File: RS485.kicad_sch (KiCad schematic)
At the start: 8 parts, among them J7 RS485, U9 XR3072XIDTR-F

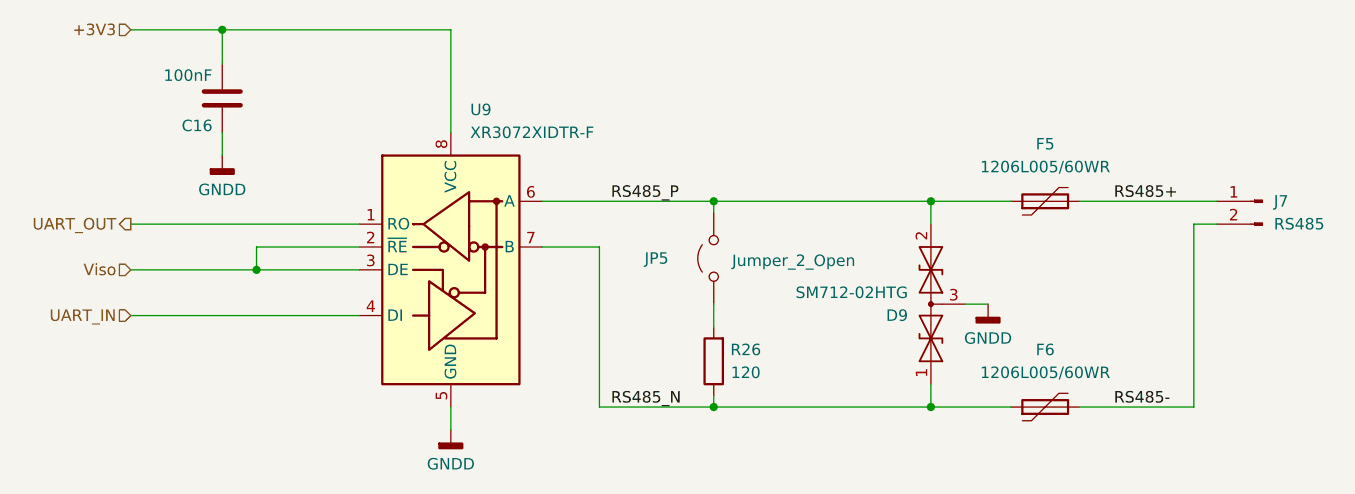
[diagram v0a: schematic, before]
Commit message: Dual SIM version
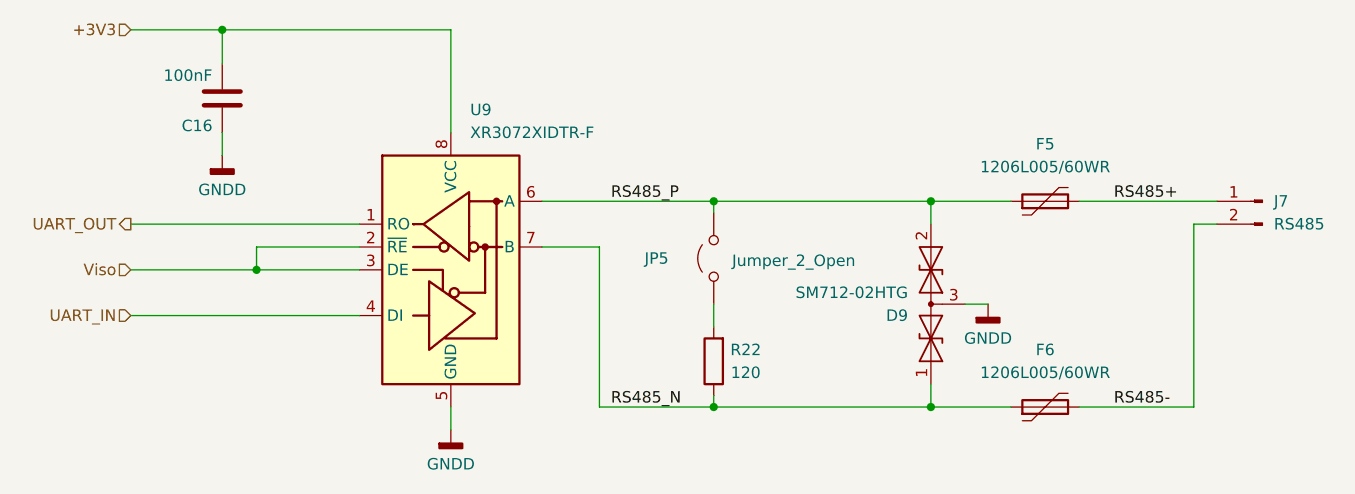
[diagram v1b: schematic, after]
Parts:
- renumbered R26 to R22
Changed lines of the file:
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@@
 		(in_pos_files yes)
 		(dnp no)
-		(property "Reference" "R26"
+		(property "Reference" "R22"
 			(at 154.686 100.33 0)
 			(show_name no)
@@
 			(project "GSMreceiver"
 				(path "/bbc92722-7b85-49e8-a662-589426df605a/fe2eac04-096c-41cd-9d48-0aafc9873100"
-					(reference "R26")
+					(reference "R22")
 					(unit 1)
 				)

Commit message: Replace SIM800C-DS with A7682E
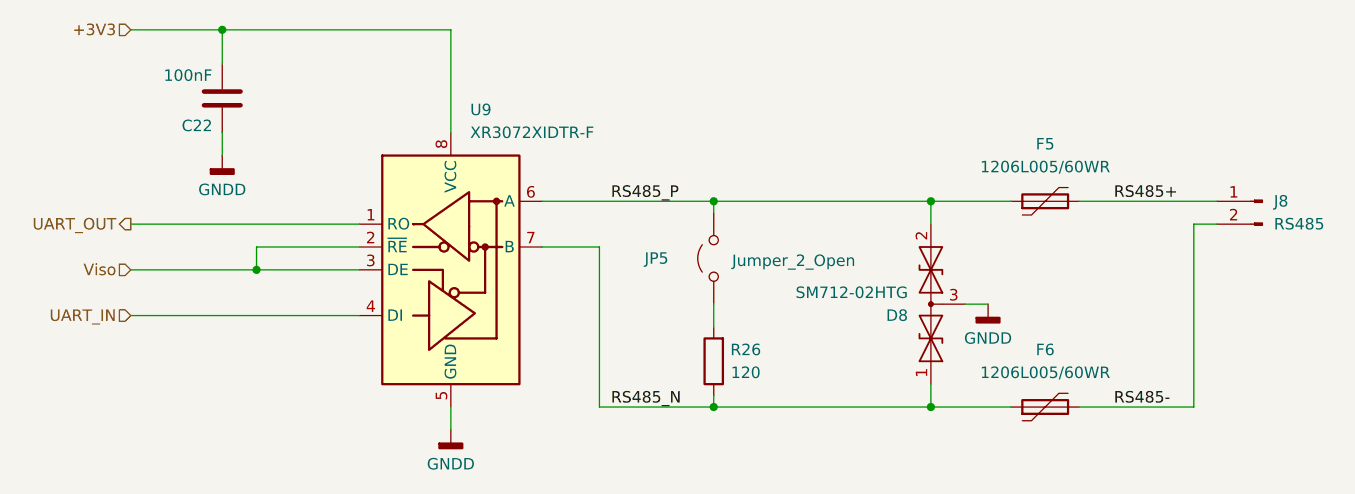
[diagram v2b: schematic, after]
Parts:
- renumbered C16 to C22, D9 to D8, J7 to J8, R22 to R26
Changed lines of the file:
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@@
 		(dnp no)
 		(fields_autoplaced yes)
-		(property "Reference" "#PWR036"
+		(property "Reference" "#PWR040"
 			(at 121.92 115.57 0)
 			(hide yes)
@@
 			(project "GSMreceiver"
 				(path "/bbc92722-7b85-49e8-a662-589426df605a/fe2eac04-096c-41cd-9d48-0aafc9873100"
-					(reference "#PWR036")
+					(reference "#PWR040")
 					(unit 1)
 				)
@@
 		(dnp no)
 		(fields_autoplaced yes)
-		(property "Reference" "D9"
+		(property "Reference" "D8"
 			(at 172.72 96.5201 90)
 			(show_name no)
@@
 			(project "GSMreceiver"
 				(path "/bbc92722-7b85-49e8-a662-589426df605a/fe2eac04-096c-41cd-9d48-0aafc9873100"
-					(reference "D9")
+					(reference "D8")
 					(unit 1)
 				)
@@
 		(in_pos_files yes)
 		(dnp no)
-		(property "Reference" "R22"
+		(property "Reference" "R26"
 			(at 154.686 100.33 0)
 			(show_name no)
@@
 			(project "GSMreceiver"
 				(path "/bbc92722-7b85-49e8-a662-589426df605a/fe2eac04-096c-41cd-9d48-0aafc9873100"
-					(reference "R22")
+					(reference "R26")
 					(unit 1)
 				)
@@
 		(dnp no)
 		(fields_autoplaced yes)
-		(property "Reference" "J7"
+		(property "Reference" "J8"
 			(at 213.36 83.8199 0)
 			(show_name no)
@@
 			(project "GSMreceiver"
 				(path "/bbc92722-7b85-49e8-a662-589426df605a/fe2eac04-096c-41cd-9d48-0aafc9873100"
-					(reference "J7")
+					(reference "J8")
 					(unit 1)
 				)
@@
 		(dnp no)
 		(fields_autoplaced yes)
-		(property "Reference" "#PWR037"
+		(property "Reference" "#PWR041"
 			(at 181.61 101.6 0)
 			(hide yes)
@@
 			(project "GSMreceiver"
 				(path "/bbc92722-7b85-49e8-a662-589426df605a/fe2eac04-096c-41cd-9d48-0aafc9873100"
-					(reference "#PWR037")
+					(reference "#PWR041")
 					(unit 1)
 				)
@@
 		(in_pos_files yes)
 		(dnp no)
-		(property "Reference" "C16"
+		(property "Reference" "C22"
 			(at 93.726 75.438 0)
 			(show_name no)
@@
 			(project "GSMreceiver"
 				(path "/bbc92722-7b85-49e8-a662-589426df605a/fe2eac04-096c-41cd-9d48-0aafc9873100"
-					(reference "C16")
+					(reference "C22")
 					(unit 1)
 				)
@@
 		(dnp no)
 		(fields_autoplaced yes)
-		(property "Reference" "#PWR035"
+		(property "Reference" "#PWR039"
 			(at 96.52 85.09 0)
 			(hide yes)
@@
 			(project "GSMreceiver"
 				(path "/bbc92722-7b85-49e8-a662-589426df605a/fe2eac04-096c-41cd-9d48-0aafc9873100"
-					(reference "#PWR035")
+					(reference "#PWR039")
 					(unit 1)
 				)

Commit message: USB connector inversion fix
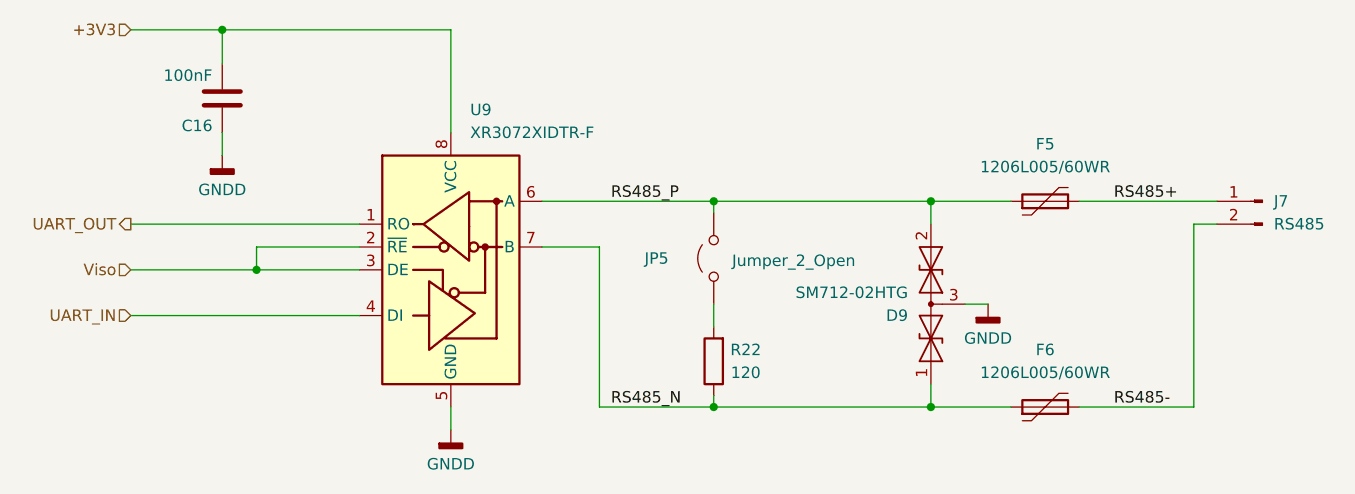
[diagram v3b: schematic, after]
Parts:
- renumbered C22 to C16, D8 to D9, J8 to J7, R26 to R22
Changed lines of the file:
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@@
 		(dnp no)
 		(fields_autoplaced yes)
-		(property "Reference" "#PWR040"
+		(property "Reference" "#PWR036"
 			(at 121.92 115.57 0)
 			(hide yes)
@@
 			(project "GSMreceiver"
 				(path "/bbc92722-7b85-49e8-a662-589426df605a/fe2eac04-096c-41cd-9d48-0aafc9873100"
-					(reference "#PWR040")
+					(reference "#PWR036")
 					(unit 1)
 				)
@@
 		(dnp no)
 		(fields_autoplaced yes)
-		(property "Reference" "D8"
+		(property "Reference" "D9"
 			(at 172.72 96.5201 90)
 			(show_name no)
@@
 			(project "GSMreceiver"
 				(path "/bbc92722-7b85-49e8-a662-589426df605a/fe2eac04-096c-41cd-9d48-0aafc9873100"
-					(reference "D8")
+					(reference "D9")
 					(unit 1)
 				)
@@
 		(in_pos_files yes)
 		(dnp no)
-		(property "Reference" "R26"
+		(property "Reference" "R22"
 			(at 154.686 100.33 0)
 			(show_name no)
@@
 			(project "GSMreceiver"
 				(path "/bbc92722-7b85-49e8-a662-589426df605a/fe2eac04-096c-41cd-9d48-0aafc9873100"
-					(reference "R26")
+					(reference "R22")
 					(unit 1)
 				)
@@
 		(dnp no)
 		(fields_autoplaced yes)
-		(property "Reference" "J8"
+		(property "Reference" "J7"
 			(at 213.36 83.8199 0)
 			(show_name no)
@@
 			(project "GSMreceiver"
 				(path "/bbc92722-7b85-49e8-a662-589426df605a/fe2eac04-096c-41cd-9d48-0aafc9873100"
-					(reference "J8")
+					(reference "J7")
 					(unit 1)
 				)
@@
 		(dnp no)
 		(fields_autoplaced yes)
-		(property "Reference" "#PWR041"
+		(property "Reference" "#PWR037"
 			(at 181.61 101.6 0)
 			(hide yes)
@@
 			(project "GSMreceiver"
 				(path "/bbc92722-7b85-49e8-a662-589426df605a/fe2eac04-096c-41cd-9d48-0aafc9873100"
-					(reference "#PWR041")
+					(reference "#PWR037")
 					(unit 1)
 				)
@@
 		(in_pos_files yes)
 		(dnp no)
-		(property "Reference" "C22"
+		(property "Reference" "C16"
 			(at 93.726 75.438 0)
 			(show_name no)
@@
 			(project "GSMreceiver"
 				(path "/bbc92722-7b85-49e8-a662-589426df605a/fe2eac04-096c-41cd-9d48-0aafc9873100"
-					(reference "C22")
+					(reference "C16")
 					(unit 1)
 				)
@@
 		(dnp no)
 		(fields_autoplaced yes)
-		(property "Reference" "#PWR039"
+		(property "Reference" "#PWR035"
 			(at 96.52 85.09 0)
 			(hide yes)
@@
 			(project "GSMreceiver"
 				(path "/bbc92722-7b85-49e8-a662-589426df605a/fe2eac04-096c-41cd-9d48-0aafc9873100"
-					(reference "#PWR039")
+					(reference "#PWR035")
 					(unit 1)
 				)
